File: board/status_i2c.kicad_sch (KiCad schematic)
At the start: 54 parts, among them J5 I2C_3V3, Q10 BC548, Q11 BC548, Q12 BC548, Q13 BC548, Q14 BC548, Q15 BC548, Q16 BC548, Q17 BC548, Q18 BC548, Q7 BC548, Q8 BC548, Q9 BC548, SW11 TD_A, SW12 TD_B, SW13 TD2_A, SW14 TD2_B, SW15 SW_DIP_x03, U10 MCP23008-xP, U11 CAT24C256, U12 MCP7940N-xP, U9 24LC1025, Y1 32.768kHz

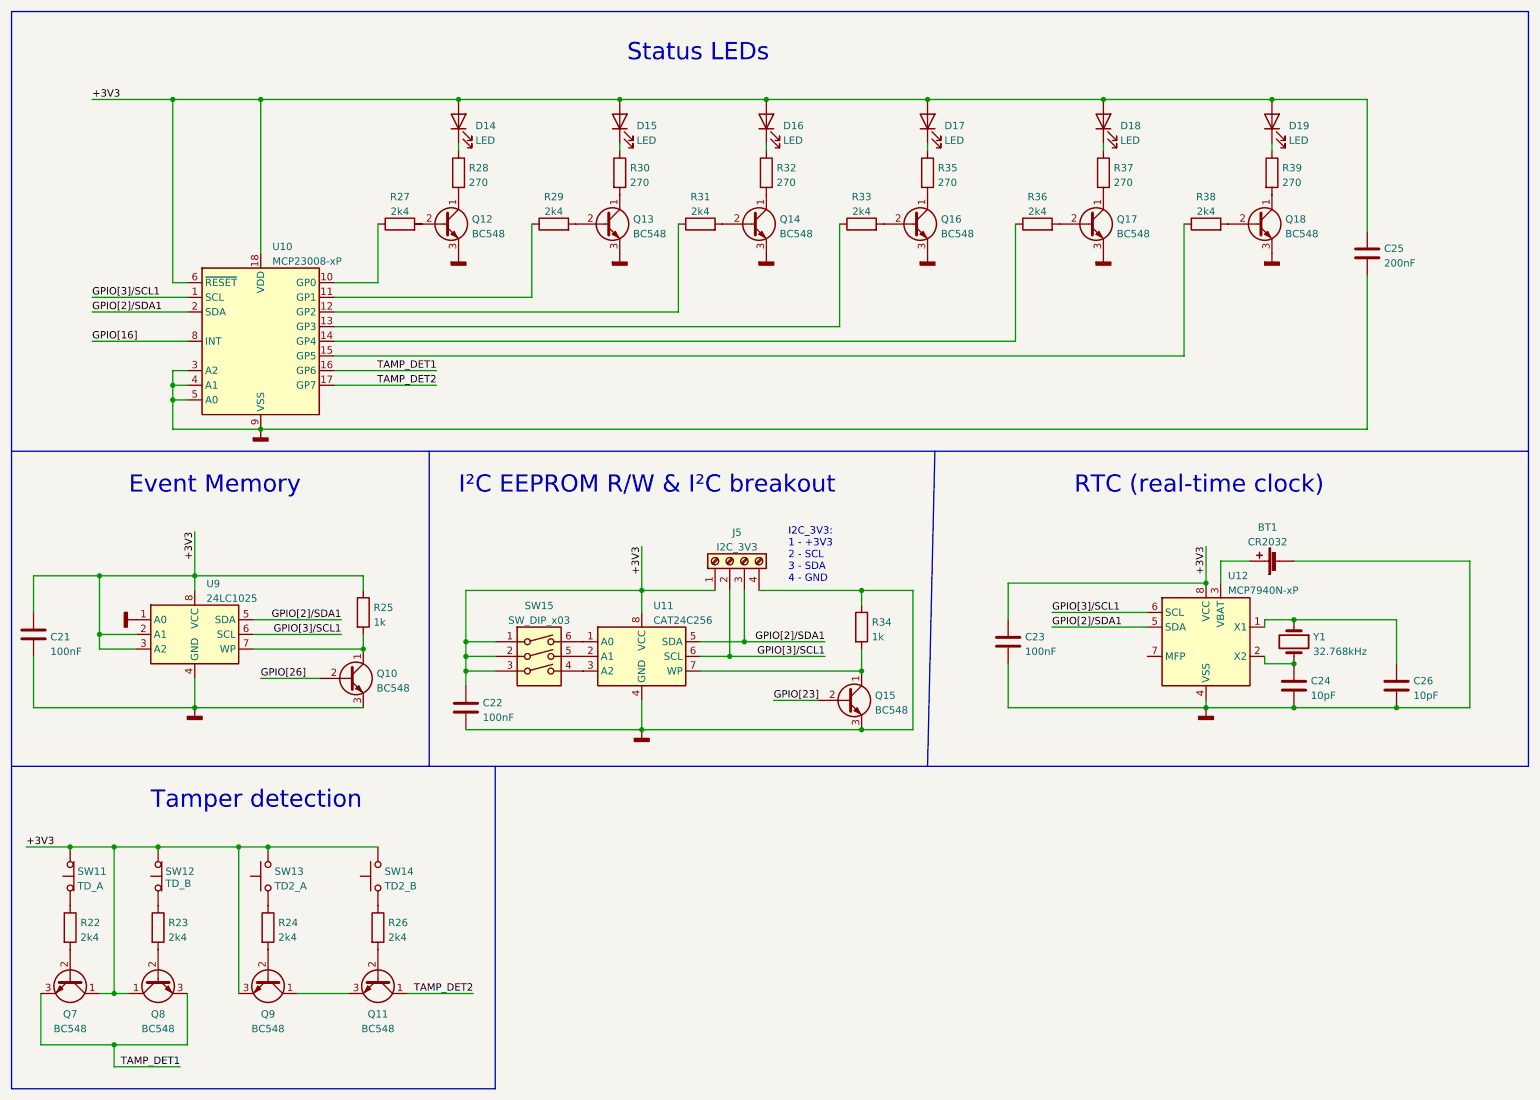
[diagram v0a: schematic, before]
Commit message: Re-structure schematics and improve safety.
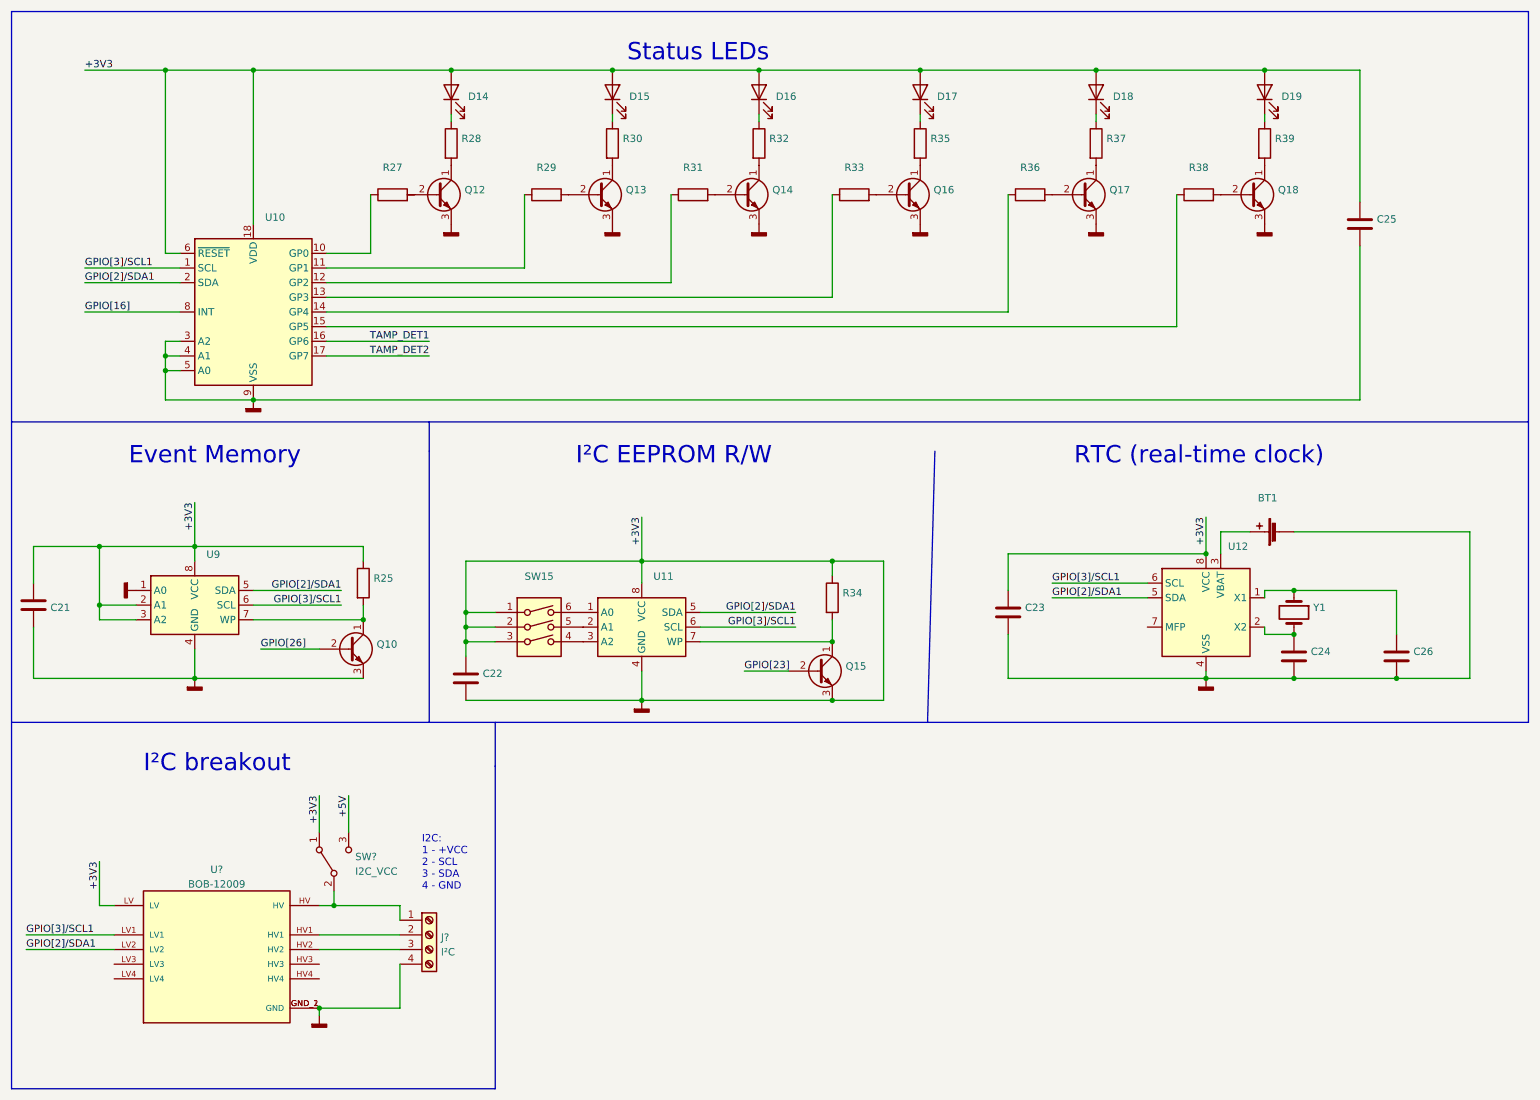
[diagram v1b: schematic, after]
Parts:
- removed J5: I2C_3V3, TerminalBlock_MetzConnect:TerminalBlock_MetzConnect_Type059_RT06304HBWC_1x04_P3.50mm_Horizontal, symbol Connector:Screw_Terminal_01x04
- removed Q11, Q7, Q8, Q9: BC548, Package_TO_SOT_THT:TO-92_Inline, symbol Transistor_BJT:BC548
- removed R22, R23, R24, R26: 2k4, symbol Device:R
- removed SW11: TD_A, symbol Switch:SW_Push_Open
- removed SW12: TD_B, symbol Switch:SW_Push_Open
- removed SW13: TD2_A, symbol Switch:SW_Push
- removed SW14: TD2_B, symbol Switch:SW_Push
- added J?: I²C, symbol Connector:Screw_Terminal_01x04
- added SW?: I2C_VCC, symbol Switch:SW_SPDT
- added U?: BOB-12009, CONV_BOB-12009, symbol BOB-12009:BOB-12009
- BT1: value CR2032 -> (none); footprint Battery:BatteryHolder_Keystone_1058_1x2032 -> (none)
- C21, C22, C23: value 100nF -> (none)
- C24, C26: value 10pF -> (none)
- C25: value 200nF -> (none)
- D14, D15, D16, D17, D18, D19: value LED -> (none)
- Q10, Q12, Q13, Q14, Q15, Q16, Q17, Q18: value BC548 -> (none); footprint Package_TO_SOT_THT:TO-92_Inline -> (none)
- R25, R34: value 1k -> (none)
- R27, R29, R31, R33, R36, R38: value 2k4 -> (none)
- R28, R30, R32, R35, R37, R39: value 270 -> (none)
- SW15: value SW_DIP_x03 -> (none); footprint Button_Switch_THT:SW_DIP_SPSTx03_Slide_9.78x9.8mm_W7.62mm_P2.54mm -> (none)
- U10: value MCP23008-xP -> (none); footprint Package_DIP:DIP-18_W7.62mm -> (none)
- U11: value CAT24C256 -> (none)
- U12: value MCP7940N-xP -> (none); footprint Package_DIP:DIP-8_W7.62mm_Socket_LongPads -> (none)
- U9: value 24LC1025 -> (none)
- Y1: value 32.768kHz -> (none)
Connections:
- net +3V3 is gone; now on net GNDD: C21.1, C22.1, C23.1, C25.1, D14.2 (A), D15.2 (A), D16.2 (A), D17.2 (A), D18.2 (A), D19.2 (A), R25.1, SW15.1, SW15.2, SW15.3, U10.18 (VDD), U10.6 (~{RESET}), U11.8 (VCC), U12.8 (VCC), U9.2 (A1), U9.3 (A2), U9.8 (VCC)
- net GNDD: now also J?.4 (Pin_4), SW?.1 (A), U?.GND_1 (GND), U?.GND_2 (GND), U?.LV
- net GPIO[2]/SDA1: now also U?.LV2
- net GPIO[3]/SCL1: now also U?.LV1
- new net: J?.1 (Pin_1), SW?.2 (B), U?.HV
- new net: J?.2 (Pin_2), U?.HV1
- new net: J?.3 (Pin_3), U?.HV2
- new net +5V: SW?.3 (C)
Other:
- note added: "I2C: 1 - +VCC 2 - SCL 3 - SDA 4 - GND"
- note added: "I²C EEPROM R/W"
- note added: "I²C breakout"
- note removed: "I2C_3V3: 1 - +3V3 2 - SCL 3 - SDA 4 - GND"
- note removed: "I²C EEPROM R/W & I²C breakout"
- note removed: "Tamper detection"
- moved on the sheet: BT1, C21, C22, C23, C24, C25, C26, D14, D15, D16, D17, D18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

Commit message: Add missing footprints.
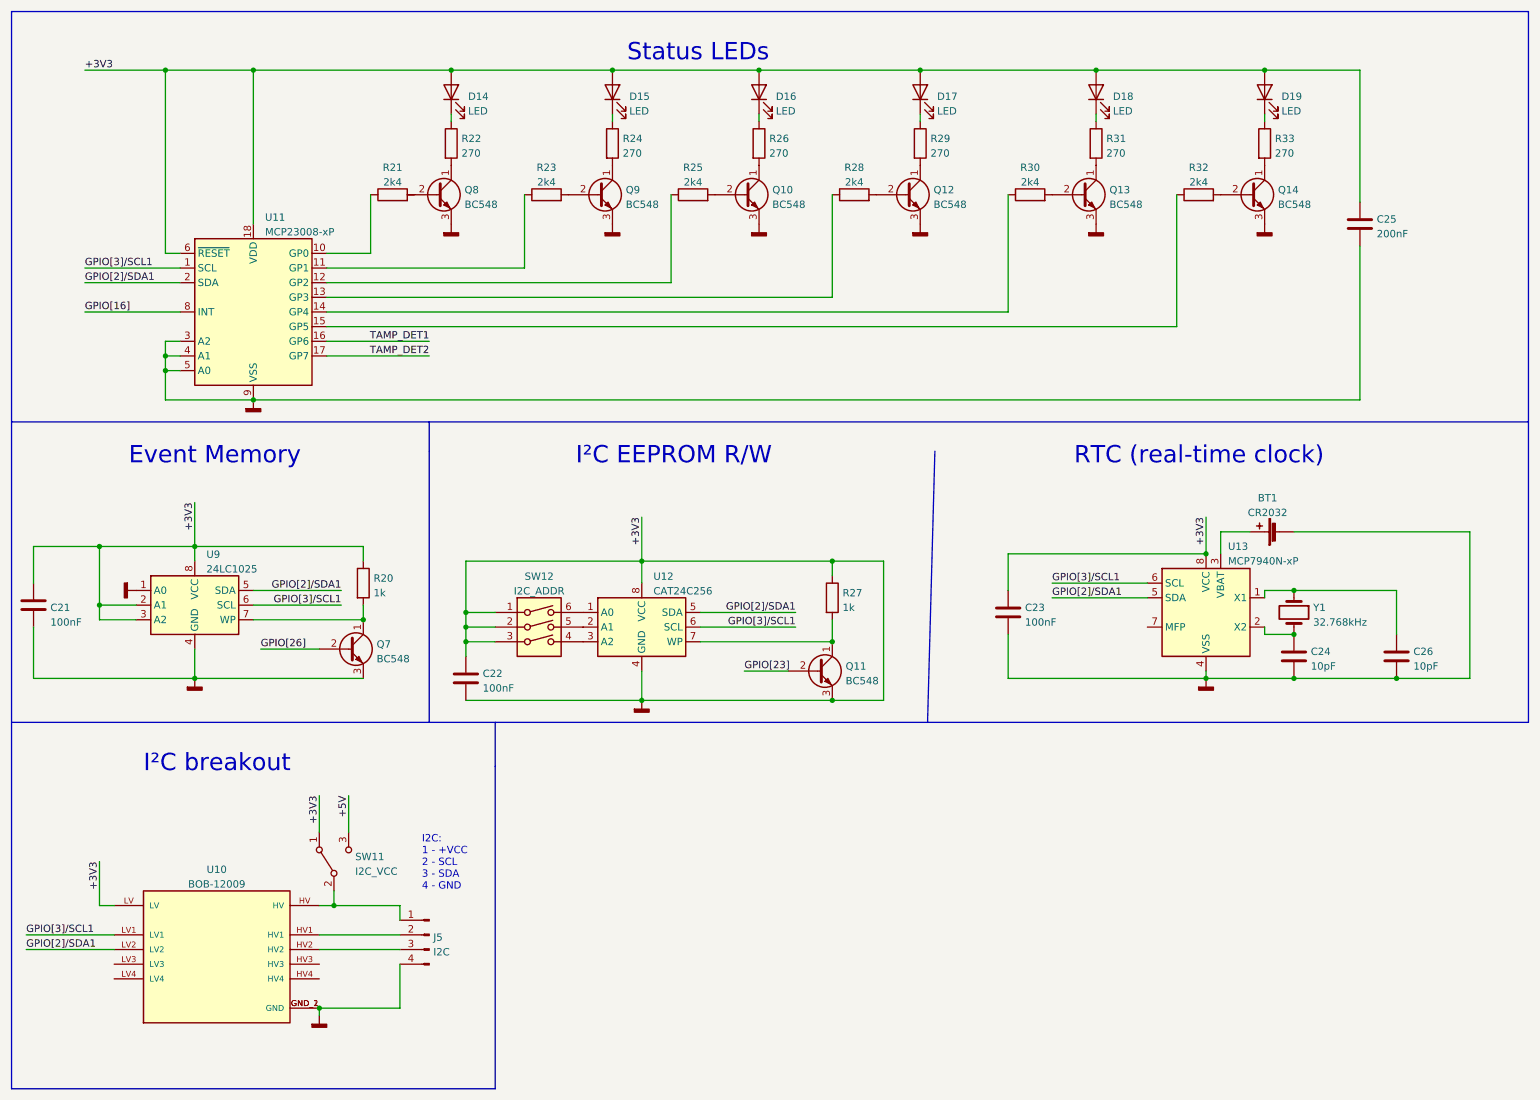
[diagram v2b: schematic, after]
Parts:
- removed J?: I²C, symbol Connector:Screw_Terminal_01x04
- added J5: I2C, Connector_PinHeader_2.54mm:PinHeader_1x04_P2.54mm_Vertical, symbol Connector:Conn_01x04_Male
- BT1: value (none) -> CR2032; footprint (none) -> Battery:BatteryHolder_Keystone_1058_1x2032
- C21, C22, C23: value (none) -> 100nF; footprint (none) -> Capacitor_THT:C_Disc_D5.0mm_W2.5mm_P5.00mm
- C24, C26: value (none) -> 10pF; footprint (none) -> Capacitor_THT:C_Radial_D6.3mm_H5.0mm_P2.50mm
- C25: value (none) -> 200nF; footprint (none) -> Capacitor_THT:C_Disc_D5.0mm_W2.5mm_P5.00mm
- D14, D15, D16, D17, D18, D19: value (none) -> LED; footprint (none) -> LED_THT:LED_D3.0mm
- Q10: renamed from Q14; value (none) -> BC548; footprint (none) -> Package_TO_SOT_THT:TO-92_Inline
- Q11: renamed from Q15; value (none) -> BC548; footprint (none) -> Package_TO_SOT_THT:TO-92_Inline
- Q12: renamed from Q16; value (none) -> BC548; footprint (none) -> Package_TO_SOT_THT:TO-92_Inline
- Q13: renamed from Q17; value (none) -> BC548; footprint (none) -> Package_TO_SOT_THT:TO-92_Inline
- Q14: renamed from Q18; value (none) -> BC548; footprint (none) -> Package_TO_SOT_THT:TO-92_Inline
- Q7: renamed from Q10; value (none) -> BC548; footprint (none) -> Package_TO_SOT_THT:TO-92_Inline
- Q8: renamed from Q12; value (none) -> BC548; footprint (none) -> Package_TO_SOT_THT:TO-92_Inline
- Q9: renamed from Q13; value (none) -> BC548; footprint (none) -> Package_TO_SOT_THT:TO-92_Inline
- R20: renamed from R25; value (none) -> 1k; footprint (none) -> Resistor_THT:R_Axial_DIN0516_L15.5mm_D5.0mm_P7.62mm_Vertical
- R21: renamed from R27; value (none) -> 2k4; footprint (none) -> Resistor_THT:R_Axial_DIN0516_L15.5mm_D5.0mm_P7.62mm_Vertical
- R22: renamed from R28; value (none) -> 270; footprint (none) -> Resistor_THT:R_Axial_DIN0516_L15.5mm_D5.0mm_P7.62mm_Vertical
- R23: renamed from R29; value (none) -> 2k4; footprint (none) -> Resistor_THT:R_Axial_DIN0516_L15.5mm_D5.0mm_P7.62mm_Vertical
- R24: renamed from R30; value (none) -> 270; footprint (none) -> Resistor_THT:R_Axial_DIN0516_L15.5mm_D5.0mm_P7.62mm_Vertical
- R25: renamed from R31; value (none) -> 2k4; footprint (none) -> Resistor_THT:R_Axial_DIN0516_L15.5mm_D5.0mm_P7.62mm_Vertical
- R26: renamed from R32; value (none) -> 270; footprint (none) -> Resistor_THT:R_Axial_DIN0516_L15.5mm_D5.0mm_P7.62mm_Vertical
- R27: renamed from R34; value (none) -> 1k; footprint (none) -> Resistor_THT:R_Axial_DIN0516_L15.5mm_D5.0mm_P7.62mm_Vertical
- R28: renamed from R33; value (none) -> 2k4; footprint (none) -> Resistor_THT:R_Axial_DIN0516_L15.5mm_D5.0mm_P7.62mm_Vertical
- R29: renamed from R35; value (none) -> 270; footprint (none) -> Resistor_THT:R_Axial_DIN0516_L15.5mm_D5.0mm_P7.62mm_Vertical
- R30: renamed from R36; value (none) -> 2k4; footprint (none) -> Resistor_THT:R_Axial_DIN0516_L15.5mm_D5.0mm_P7.62mm_Vertical
- R31: renamed from R37; value (none) -> 270; footprint (none) -> Resistor_THT:R_Axial_DIN0516_L15.5mm_D5.0mm_P7.62mm_Vertical
- R32: renamed from R38; value (none) -> 2k4; footprint (none) -> Resistor_THT:R_Axial_DIN0516_L15.5mm_D5.0mm_P7.62mm_Vertical
- R33: renamed from R39; value (none) -> 270; footprint (none) -> Resistor_THT:R_Axial_DIN0516_L15.5mm_D5.0mm_P7.62mm_Vertical
- SW11: renamed from SW?; footprint (none) -> Button_Switch_THT:SW_CuK_OS102011MA1QN1_SPDT_Angled
- SW12: renamed from SW15; value (none) -> I2C_ADDR; footprint (none) -> Button_Switch_THT:SW_DIP_SPSTx03_Slide_9.78x9.8mm_W7.62mm_P2.54mm
- U10: renamed from U?; footprint CONV_BOB-12009 -> BOB-12009:CONV_BOB-12009
- U11: renamed from U10; value (none) -> MCP23008-xP; footprint (none) -> Package_DIP:DIP-18_W7.62mm
- U12: renamed from U11; value (none) -> CAT24C256; footprint (none) -> Package_DIP:DIP-8_W7.62mm_Socket_LongPads
- U13: renamed from U12; value (none) -> MCP7940N-xP; footprint (none) -> Package_DIP:DIP-8_W7.62mm_Socket_LongPads
- U9: value (none) -> 24LC1025; footprint (none) -> Package_DIP:DIP-8_W7.62mm_Socket_LongPads
- Y1: value (none) -> 32.768kHz; footprint (none) -> Crystal:Crystal_C26-LF_D2.1mm_L6.5mm_Vertical
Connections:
- net GNDD: now also J5.4 (Pin_4)
- net at SW11.2 (B), U10.HV: now also J5.1 (Pin_1)
- net at U10.HV1: now also J5.2 (Pin_2)
- net at U10.HV2: now also J5.3 (Pin_3)
